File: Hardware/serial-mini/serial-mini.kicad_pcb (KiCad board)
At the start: 2 copper layers, 7.1 x 1.2 mm, 52 parts, among them J1 PICKIT_V3_HEADER, J2 10118193-0001LF, J3 3-106505-2, Q1 IRLML2060, Q2 IRLML2060, Q3 IRLML2060, U1 SIT2001BI-S2-33S-100.000000D, U2 FT230XQ-R, U3 DSPIC33CK64MP105, U4 SN74AHC14RGYR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

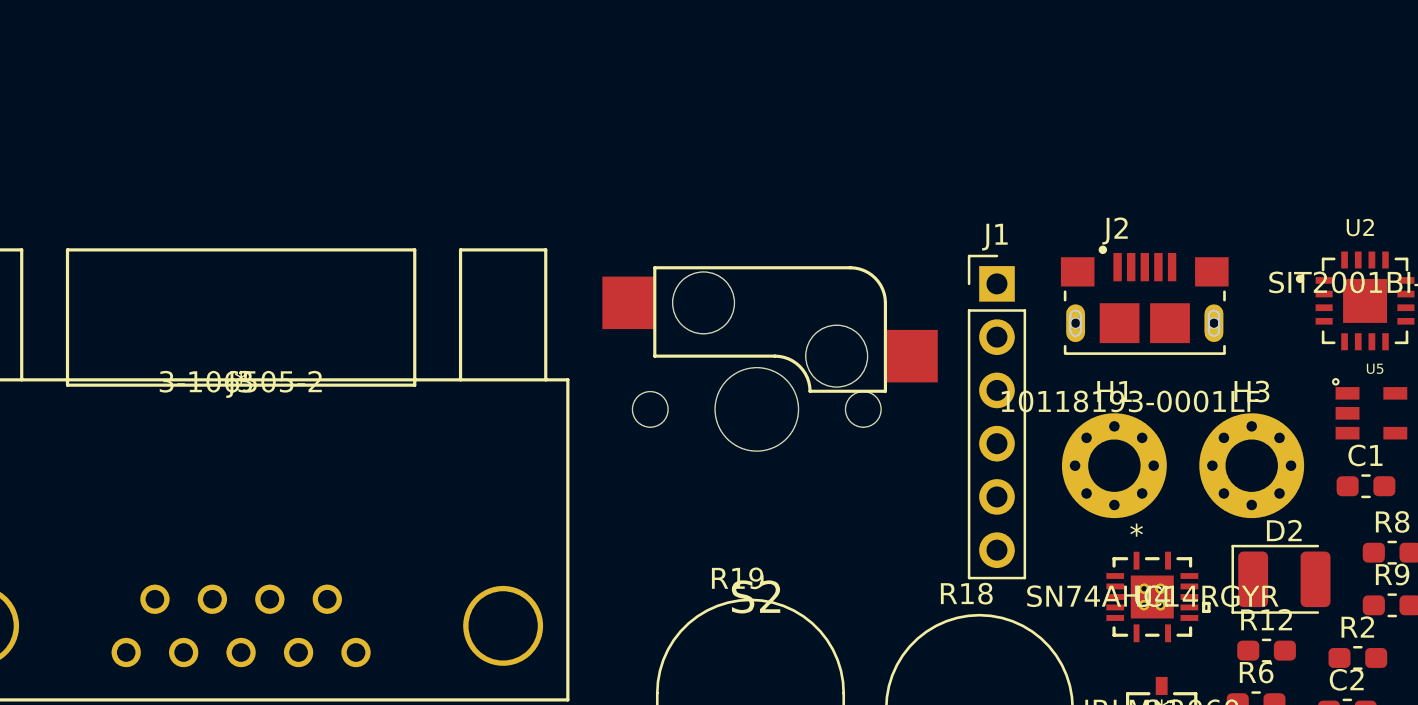
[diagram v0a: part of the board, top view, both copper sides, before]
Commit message: Update symbols/footprints
Linked most symbols to their datasheets, updated more footprint/symbol footprints.
Also added status indicator LED
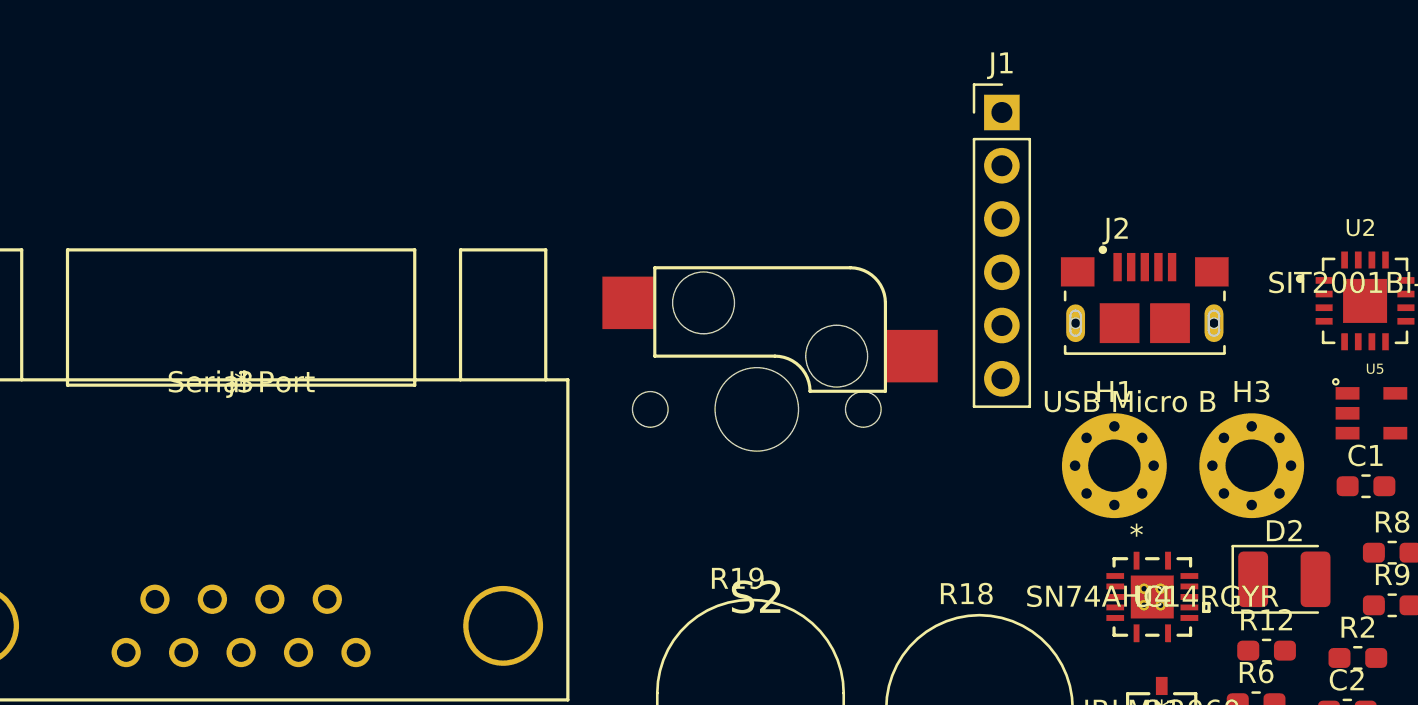
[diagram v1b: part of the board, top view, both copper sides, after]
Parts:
- J1: value PICKIT_V3_HEADER -> PICKIT V3 Header; footprint Connector_PinHeader_2.54mm:PinHeader_1x06_P2.54mm_Vertical -> serial-mini:PICKITv3
- J2: value 10118193-0001LF -> USB Micro B
- J3: value 3-106505-2 -> Serial Port
- U3: value DSPIC33CK64MP105 -> DSPIC33CK64MP102
- moved J1 8.18 mm to (125.7, -20.3)
